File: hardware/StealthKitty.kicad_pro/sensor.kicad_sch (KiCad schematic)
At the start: 11 parts, among them J1 Conn_01x08, J7 Conn_01x06, J9 Conn_01x06, U5 ADXL343

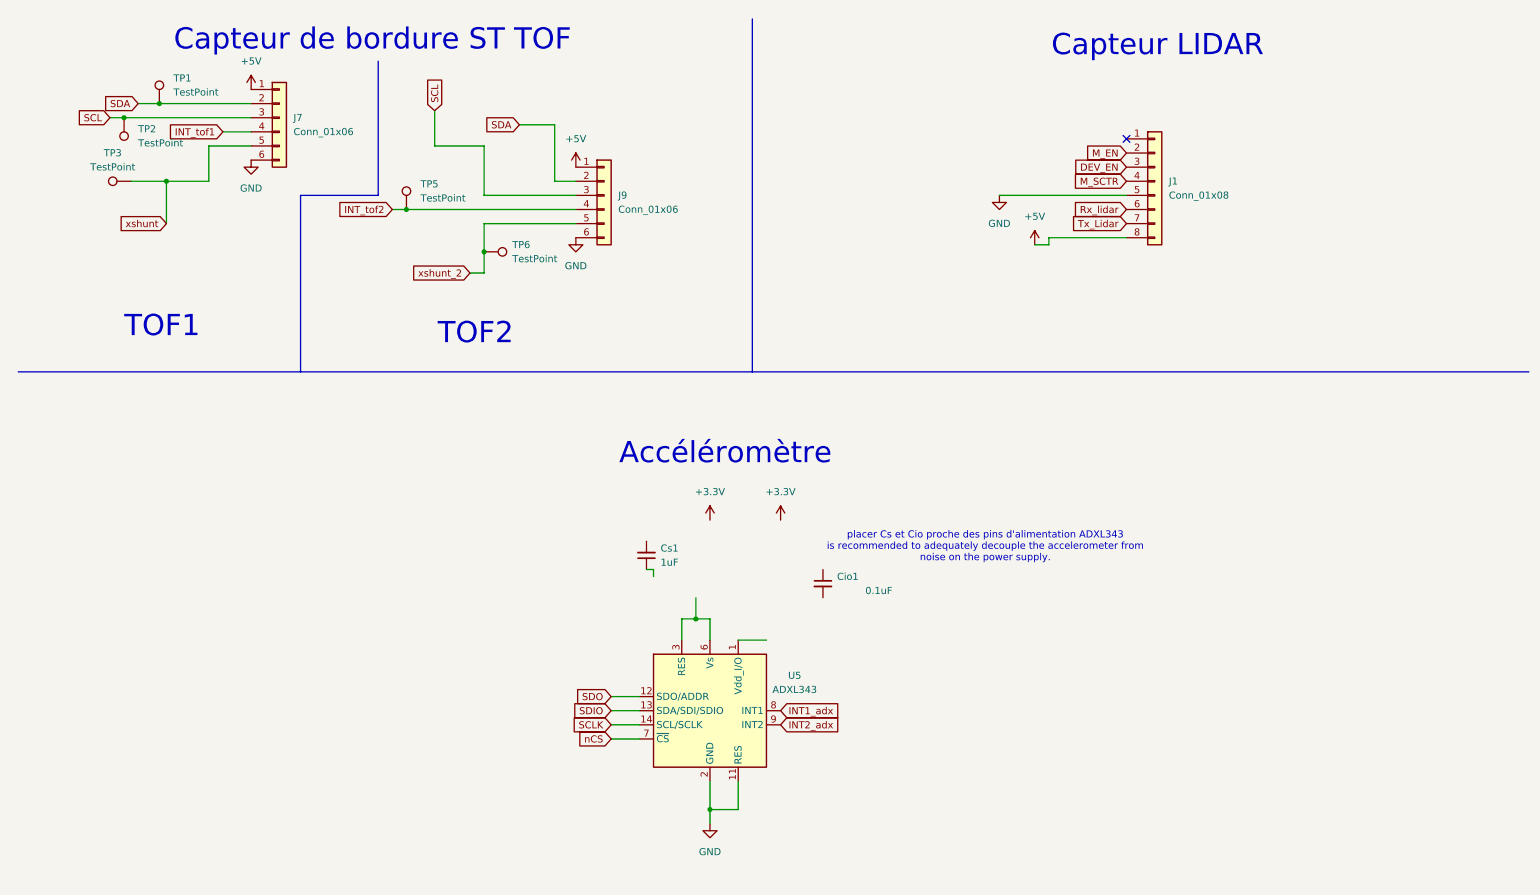
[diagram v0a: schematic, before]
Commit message: réassignation pins stm32, ajout des modifs de la partie power, ajout des modfis de la revue de projet 02/10/24, modifs du 3/10/24 voir readme
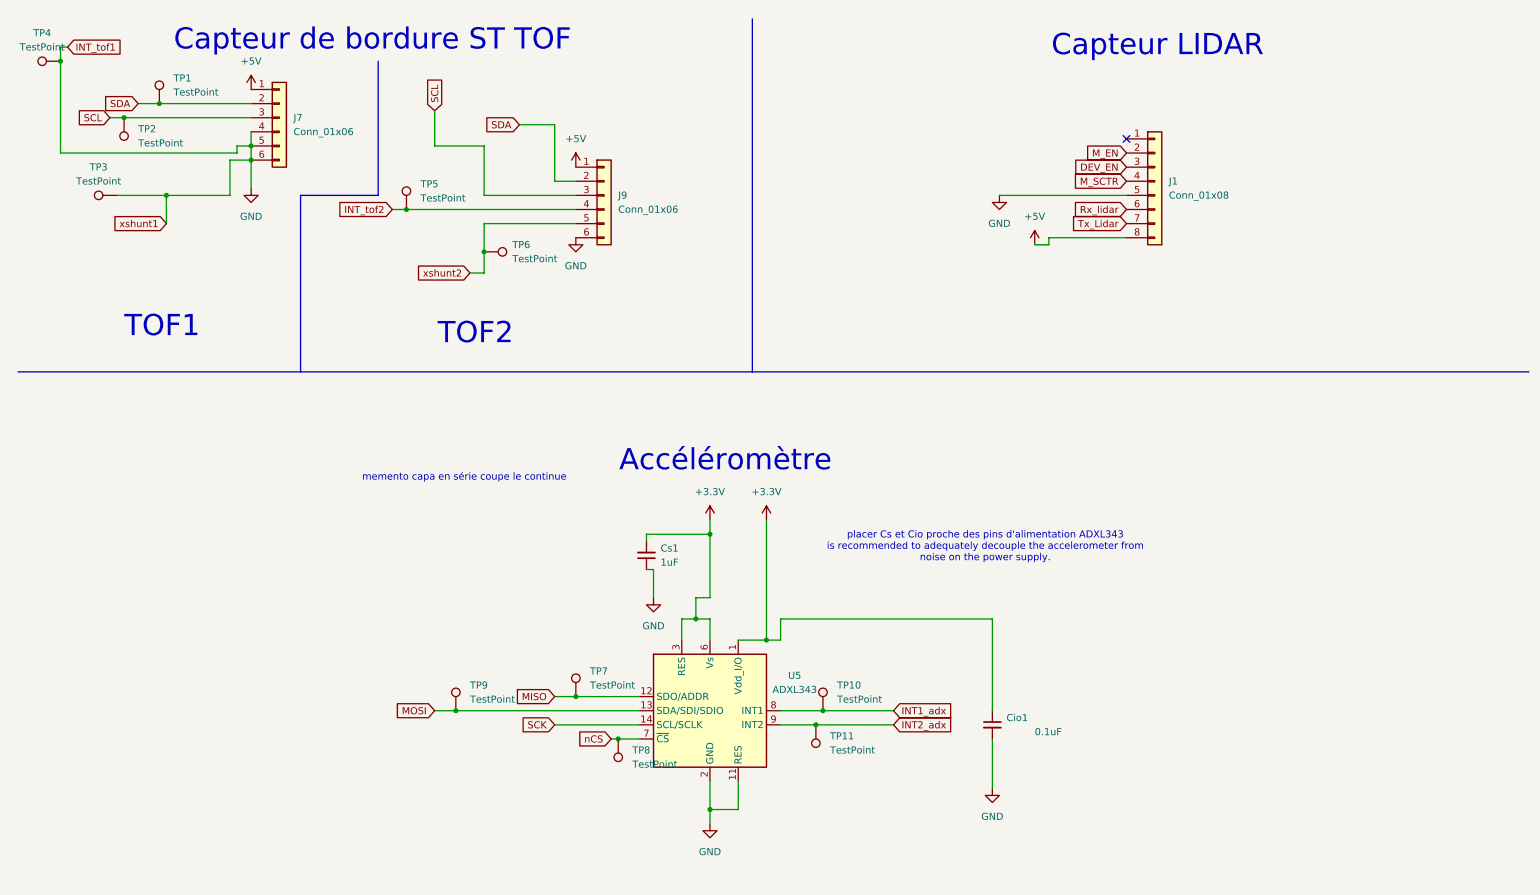
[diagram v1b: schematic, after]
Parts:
- added TP10, TP11, TP4, TP7, TP8, TP9: TestPoint, TestPoint:TestPoint_Pad_D1.5mm, symbol Connector:TestPoint
- TP1, TP2, TP3, TP5, TP6: footprint (none) -> TestPoint:TestPoint_Pad_D1.5mm
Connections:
- net INT_tof1 is gone; now on net GND: J7.4 (Pin_4)
- net xshunt is gone; now on net GND: J7.5 (Pin_5), TP3.1
- net +3.3V: now also Cio1.1, Cs1.2, U5.1 (Vdd_I/O), U5.3 (RES), U5.6 (Vs)
- net GND: now also Cio1.2, Cs1.1, TP4.1
- net INT1_adx: now also TP10.1
- net INT2_adx: now also TP11.1
- net nCS: now also TP8.1
- net SCLK renamed SCK
- net SDIO renamed MOSI
- net MOSI: now also TP9.1
- net SDO renamed MISO
- net MISO: now also TP7.1
- net xshunt_2 renamed xshunt2
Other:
- note added: "memento capa en série coupe le continue"
- moved on the sheet: Cio1, TP3

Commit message: MAJ routage equipe
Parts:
- removed TP8: TestPoint, TestPoint:TestPoint_Pad_D1.5mm, symbol Connector:TestPoint
- Cio1: footprint (none) -> Capacitor_SMD:C_0402_1005Metric_Pad0.74x0.62mm_HandSolder
- Cs1: footprint (none) -> Capacitor_SMD:C_0603_1608Metric_Pad1.08x0.95mm_HandSolder
- J7, J9: footprint (none) -> Connector_JST:JST_XH_B6B-XH-A_1x06_P2.50mm_Vertical
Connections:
- net GND: no longer J7.4 (Pin_4), J7.5 (Pin_5), TP3.1, TP4.1
- new net INT_tof1: J7.4 (Pin_4), TP4.1
- new net xshunt1: J7.5 (Pin_5), TP3.1
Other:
- moved on the sheet: Cio1, J7, J9, TP1, TP2, TP3, TP4, TP5, TP6, TP9

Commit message: Confirmation placement equipe
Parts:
- renumbered Cio1 to Cio301, Cs1 to Cs301, J7 to J301, J9 to J302, J1 to J303, TP4 to TP301, TP3 to TP302, TP1 to TP303, TP2 to TP304, TP5 to TP305, TP6 to TP306, TP7 to TP307, TP9 to TP308, TP11 to TP309, TP10 to TP310, U5 to U301
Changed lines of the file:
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@@
 		(dnp no)
 		(fields_autoplaced yes)
-		(property "Reference" "#PWR061"
+		(property "Reference" "#PWR0308"
 			(at 142.24 106.68 0)
 			(effects
@@
 			(project "StealthKitty.kicad_pro"
 				(path "/23d5732b-7ccb-40aa-85a2-3b18421ac23b/8cd8413a-9ba4-4bd6-b413-2331caa50cc2"
-					(reference "#PWR061")
+					(reference "#PWR0308")
 					(unit 1)
 				)
@@
 		(on_board yes)
 		(dnp no)
-		(property "Reference" "TP1"
+		(property "Reference" "TP303"
 			(at 48.006 23.876 0)
 			(effects
@@
 			(project "StealthKitty.kicad_pro"
 				(path "/23d5732b-7ccb-40aa-85a2-3b18421ac23b/8cd8413a-9ba4-4bd6-b413-2331caa50cc2"
-					(reference "TP1")
+					(reference "TP303")
 					(unit 1)
 				)
@@
 		(dnp no)
 		(fields_autoplaced yes)
-		(property "Reference" "TP7"
+		(property "Reference" "TP307"
 			(at 115.57 130.0479 0)
 			(effects
@@
 			(project "StealthKitty.kicad_pro"
 				(path "/23d5732b-7ccb-40aa-85a2-3b18421ac23b/8cd8413a-9ba4-4bd6-b413-2331caa50cc2"
-					(reference "TP7")
+					(reference "TP307")
 					(unit 1)
 				)
@@
 		(dnp no)
 		(fields_autoplaced yes)
-		(property "Reference" "#PWR01"
+		(property "Reference" "#PWR0302"
 			(at 58.42 53.34 0)
 			(effects
@@
 			(project "StealthKitty.kicad_pro"
 				(path "/23d5732b-7ccb-40aa-85a2-3b18421ac23b/8cd8413a-9ba4-4bd6-b413-2331caa50cc2"
-					(reference "#PWR01")
+					(reference "#PWR0302")
 					(unit 1)
 				)
@@
 		(on_board yes)
 		(dnp no)
-		(property "Reference" "TP2"
+		(property "Reference" "TP304"
 			(at 44.45 35.814 0)
 			(effects
@@
 			(project "StealthKitty.kicad_pro"
 				(path "/23d5732b-7ccb-40aa-85a2-3b18421ac23b/8cd8413a-9ba4-4bd6-b413-2331caa50cc2"
-					(reference "TP2")
+					(reference "TP304")
 					(unit 1)
 				)
@@
 		(on_board yes)
 		(dnp no)
-		(property "Reference" "#PWR023"
+		(property "Reference" "#PWR0301"
 			(at 54.61 33.02 0)
 			(effects
@@
 			(project "StealthKitty.kicad_pro"
 				(path "/23d5732b-7ccb-40aa-85a2-3b18421ac23b/8cd8413a-9ba4-4bd6-b413-2331caa50cc2"
-					(reference "#PWR023")
+					(reference "#PWR0301")
 					(unit 1)
 				)
@@
 		(dnp no)
 		(fields_autoplaced yes)
-		(property "Reference" "J9"
+		(property "Reference" "J302"
 			(at 130.81 34.2899 0)
 			(effects
@@
 			(project "StealthKitty.kicad_pro"
 				(path "/23d5732b-7ccb-40aa-85a2-3b18421ac23b/8cd8413a-9ba4-4bd6-b413-2331caa50cc2"
-					(reference "J9")
+					(reference "J302")
 					(unit 1)
 				)
@@
 		(dnp no)
 		(fields_autoplaced yes)
-		(property "Reference" "#PWR060"
+		(property "Reference" "#PWR0304"
 			(at 123.19 48.26 0)
 			(effects
@@
 			(project "StealthKitty.kicad_pro"
 				(path "/23d5732b-7ccb-40aa-85a2-3b18421ac23b/8cd8413a-9ba4-4bd6-b413-2331caa50cc2"
-					(reference "#PWR060")
+					(reference "#PWR0304")
 					(unit 1)
 				)
@@
 		(dnp no)
 		(fields_autoplaced yes)
-		(property "Reference" "J1"
+		(property "Reference" "J303"
 			(at 219.71 41.9099 0)
 			(effects
@@
 			(project "StealthKitty.kicad_pro"
 				(path "/23d5732b-7ccb-40aa-85a2-3b18421ac23b/8cd8413a-9ba4-4bd6-b413-2331caa50cc2"
-					(reference "J1")
+					(reference "J303")
 					(unit 1)
 				)
@@
 		(dnp no)
 		(fields_autoplaced yes)
-		(property "Reference" "#PWR022"
+		(property "Reference" "#PWR0311"
 			(at 195.58 55.88 0)
 			(effects
@@
 			(project "StealthKitty.kicad_pro"
 				(path "/23d5732b-7ccb-40aa-85a2-3b18421ac23b/8cd8413a-9ba4-4bd6-b413-2331caa50cc2"
-					(reference "#PWR022")
+					(reference "#PWR0311")
 					(unit 1)
 				)
@@
 		(dnp no)
 		(fields_autoplaced yes)
-		(property "Reference" "TP6"
+		(property "Reference" "TP306"
 			(at 105.41 46.4819 0)
 			(effects
@@
 			(project "StealthKitty.kicad_pro"
 				(path "/23d5732b-7ccb-40aa-85a2-3b18421ac23b/8cd8413a-9ba4-4bd6-b413-2331caa50cc2"
-					(reference "TP6")
+					(reference "TP306")
 					(unit 1)
 				)
@@
 		(dnp no)
 		(fields_autoplaced yes)
-		(property "Reference" "TP10"
+		(property "Reference" "TP310"
 			(at 160.02 132.5879 0)
 			(effects
@@
 			(project "StealthKitty.kicad_pro"
 				(path "/23d5732b-7ccb-40aa-85a2-3b18421ac23b/8cd8413a-9ba4-4bd6-b413-2331caa50cc2"
-					(reference "TP10")
+					(reference "TP310")
 					(unit 1)
 				)
@@
 		(dnp no)
 		(fields_autoplaced yes)
-		(property "Reference" "#PWR059"
+		(property "Reference" "#PWR0303"
 			(at 123.19 33.02 0)
 			(effects
@@
 			(project "StealthKitty.kicad_pro"
 				(path "/23d5732b-7ccb-40aa-85a2-3b18421ac23b/8cd8413a-9ba4-4bd6-b413-2331caa50cc2"
-					(reference "#PWR059")
+					(reference "#PWR0303")
 					(unit 1)
 				)
@@
 		(dnp no)
 		(fields_autoplaced yes)
-		(property "Reference" "#PWR062"
+		(property "Reference" "#PWR0310"
 			(at 189.23 50.8 0)
 			(effects
@@
 			(project "StealthKitty.kicad_pro"
 				(path "/23d5732b-7ccb-40aa-85a2-3b18421ac23b/8cd8413a-9ba4-4bd6-b413-2331caa50cc2"
-					(reference "#PWR062")
+					(reference "#PWR0310")
 					(unit 1)
 				)
@@
 		(on_board yes)
 		(dnp no)
-		(property "Reference" "TP3"
+		(property "Reference" "TP302"
 			(at 29.464 51.054 0)
 			(effects
@@
 			(project "StealthKitty.kicad_pro"
 				(path "/23d5732b-7ccb-40aa-85a2-3b18421ac23b/8cd8413a-9ba4-4bd6-b413-2331caa50cc2"
-					(reference "TP3")
+					(reference "TP302")
 					(unit 1)
 				)
@@
 		(dnp no)
 		(fields_autoplaced yes)
-		(property "Reference" "U5"
+		(property "Reference" "U301"
 			(at 152.4 130.8414 0)
 			(effects
@@
 			(project "StealthKitty.kicad_pro"
 				(path "/23d5732b-7ccb-40aa-85a2-3b18421ac23b/8cd8413a-9ba4-4bd6-b413-2331caa50cc2"
-					(reference "U5")
+					(reference "U301")
 					(unit 1)
 				)
@@
 		(dnp no)
 		(fields_autoplaced yes)
-		(property "Reference" "J7"
+		(property "Reference" "J301"
 			(at 66.04 34.2899 0)
 			(effects
@@
 			(project "StealthKitty.kicad_pro"
 				(path "/23d5732b-7ccb-40aa-85a2-3b18421ac23b/8cd8413a-9ba4-4bd6-b413-2331caa50cc2"
-					(reference "J7")
+					(reference "J301")
 					(unit 1)
 				)
@@
 		(dnp no)
 		(fields_autoplaced yes)
-		(property "Reference" "#PWR058"
+		(property "Reference" "#PWR0307"
 			(at 137.16 163.83 0)
 			(effects
@@
 			(project "StealthKitty.kicad_pro"
 				(path "/23d5732b-7ccb-40aa-85a2-3b18421ac23b/8cd8413a-9ba4-4bd6-b413-2331caa50cc2"
-					(reference "#PWR058")
+					(reference "#PWR0307")
 					(unit 1)
 				)
@@
 		(dnp no)
 		(fields_autoplaced yes)
-		(property "Reference" "#PWR035"
+		(property "Reference" "#PWR0305"
 			(at 125.73 121.92 0)
 			(effects
@@
 			(project "StealthKitty.kicad_pro"
 				(path "/23d5732b-7ccb-40aa-85a2-3b18421ac23b/8cd8413a-9ba4-4bd6-b413-2331caa50cc2"
-					(reference "#PWR035")
+					(reference "#PWR0305")
 					(unit 1)
 				)
@@
 		(on_board yes)
 		(dnp no)
-		(property "Reference" "TP9"
+		(property "Reference" "TP308"
 			(at 118.364 148.082 0)
 			(effects
@@
 			(project "StealthKitty.kicad_pro"
 				(path "/23d5732b-7ccb-40aa-85a2-3b18421ac23b/8cd8413a-9ba4-4bd6-b413-2331caa50cc2"
-					(reference "TP9")
+					(reference "TP308")
 					(unit 1)
 				)
@@
 		(dnp no)
 		(fields_autoplaced yes)
-		(property "Reference" "#PWR025"
+		(property "Reference" "#PWR0306"
 			(at 134.62 106.68 0)
 			(effects
@@
 			(project "StealthKitty.kicad_pro"
 				(path "/23d5732b-7ccb-40aa-85a2-3b18421ac23b/8cd8413a-9ba4-4bd6-b413-2331caa50cc2"
-					(reference "#PWR025")
+					(reference "#PWR0306")
 					(unit 1)
 				)
@@
 		(on_board yes)
 		(dnp no)
-		(property "Reference" "Cs1"
+		(property "Reference" "Cs301"
 			(at 128.27 107.9435 0)
 			(effects
@@
 			(project "StealthKitty.kicad_pro"
 				(path "/23d5732b-7ccb-40aa-85a2-3b18421ac23b/8cd8413a-9ba4-4bd6-b413-2331caa50cc2"
-					(reference "Cs1")
+					(reference "Cs301")
 					(unit 1)
 				)
@@
 		(on_board yes)
 		(dnp no)
-		(property "Reference" "TP5"
+		(property "Reference" "TP305"
 			(at 98.298 28.448 0)
 			(effects
@@
 			(project "StealthKitty.kicad_pro"
 				(path "/23d5732b-7ccb-40aa-85a2-3b18421ac23b/8cd8413a-9ba4-4bd6-b413-2331caa50cc2"
-					(reference "TP5")
+					(reference "TP305")
 					(unit 1)
 				)
@@
 		(on_board yes)
 		(dnp no)
-		(property "Reference" "Cio1"
+		(property "Reference" "Cio301"
 			(at 154.94 107.9562 0)
 			(effects
@@
 			(project "StealthKitty.kicad_pro"
 				(path "/23d5732b-7ccb-40aa-85a2-3b18421ac23b/8cd8413a-9ba4-4bd6-b413-2331caa50cc2"
-					(reference "Cio1")
+					(reference "Cio301")
 					(unit 1)
 				)
@@
 		(on_board yes)
 		(dnp no)
-		(property "Reference" "TP4"
+		(property "Reference" "TP301"
 			(at 31.242 34.544 0)
 			(effects
@@
 			(project "StealthKitty.kicad_pro"
 				(path "/23d5732b-7ccb-40aa-85a2-3b18421ac23b/8cd8413a-9ba4-4bd6-b413-2331caa50cc2"
-					(reference "TP4")
+					(reference "TP301")
 					(unit 1)
 				)
@@
 		(dnp no)
 		(fields_autoplaced yes)
-		(property "Reference" "TP11"
+		(property "Reference" "TP309"
 			(at 158.75 141.7319 0)
 			(effects
@@
 			(project "StealthKitty.kicad_pro"
 				(path "/23d5732b-7ccb-40aa-85a2-3b18421ac23b/8cd8413a-9ba4-4bd6-b413-2331caa50cc2"
-					(reference "TP11")
+					(reference "TP309")
 					(unit 1)
 				)
@@
 		(dnp no)
 		(fields_autoplaced yes)
-		(property "Reference" "#PWR034"
+		(property "Reference" "#PWR0309"
 			(at 152.4 121.92 0)
 			(effects
@@
 			(project "StealthKitty.kicad_pro"
 				(path "/23d5732b-7ccb-40aa-85a2-3b18421ac23b/8cd8413a-9ba4-4bd6-b413-2331caa50cc2"
-					(reference "#PWR034")
-					(unit 1)
-				)
+					(reference "#PWR0309")
+					(unit 1)
+				)

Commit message: Dernier Modif 08/10/2024
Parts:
- removed TP303, TP304, TP306: TestPoint, TestPoint:TestPoint_Pad_D1.5mm, symbol Connector:TestPoint
- Cio301: footprint Capacitor_SMD:C_0402_1005Metric_Pad0.74x0.62mm_HandSolder -> Capacitor_SMD:C_0402_1005Metric
- Cs301: footprint Capacitor_SMD:C_0603_1608Metric_Pad1.08x0.95mm_HandSolder -> Capacitor_SMD:C_0402_1005Metric
- J301, J302: footprint Connector_JST:JST_XH_B6B-XH-A_1x06_P2.50mm_Vertical -> Connector_JST:JST_XH_S6B-XH-A_1x06_P2.50mm_Horizontal
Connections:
- net INT_tof1: no longer TP301.1
- net SCK: now also TP301.1
- net nCS: now also TP302.1
- net xshunt1: no longer TP302.1
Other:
- moved on the sheet: TP308

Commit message: Modification Placement 09/10/24
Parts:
- removed TP305: TestPoint, TestPoint:TestPoint_Pad_D1.5mm, symbol Connector:TestPoint
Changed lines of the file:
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@@
-	)
-	(junction
-		(at 102.87 36.83)
-		(diameter 0)
-		(color 0 0 0 0)
 	)
 	(junction
@@
 	(wire
 		(pts
-			(xy 102.87 36.83) (xy 123.19 36.83)
+			(xy 99.06 36.83) (xy 123.19 36.83)
 		)
 		(stroke
@@
 	(wire
 		(pts
-			(xy 99.06 36.83) (xy 102.87 36.83)
-		)
-		(stroke
-			(width 0)
-			(type default)
-		)
-	)
-	(wire
-		(pts
 			(xy 110.49 29.21) (xy 110.49 34.29)
 		)
@@
 		(pts
 			(xy 52.07 39.37) (xy 58.42 39.37)
-		)
-		(stroke
-			(width 0)
-			(type default)
-		)
-	)
-	(wire
-		(pts
-			(xy 102.87 33.02) (xy 102.87 36.83)
 		)
 		(stroke
@@
 					(unit 1)
 				)
-			)
-		)
-	)
-	(symbol
-		(lib_id "Connector:TestPoint")
-		(at 102.87 33.02 0)
-		(unit 1)
-		(exclude_from_sim no)
-		(in_bom yes)
-		(on_board yes)
-		(dnp no)
-		(property "Reference" "TP305"
-			(at 98.298 28.448 0)
-			(effects
-				(font
-					(size 1.27 1.27)
-				)
-				(justify left)
-			)
-		)
-		(property "Value" "TestPoint"
-			(at 92.964 30.988 0)
-			(effects
-				(font
-					(size 1.27 1.27)
-				)
-				(justify left)
-			)
-		)
-		(property "Footprint" "TestPoint:TestPoint_Pad_D1.5mm"
-			(at 107.95 33.02 0)
-			(effects
-				(font
-					(size 1.27 1.27)
-				)
-				(hide yes)
-			)
-		)
-		(property "Datasheet" "~"
-			(at 107.95 33.02 0)
-			(effects
-				(font
-					(size 1.27 1.27)
-				)
-				(hide yes)
-			)
-		)
-		(property "Description" "test point"
-			(at 102.87 33.02 0)
-			(effects
-				(font
-					(size 1.27 1.27)
-				)
-				(hide yes)
-			)
-		)
-		(pin "1"
-		)
-		(instances
-			(project "StealthKitty.kicad_pro"
-				(path "/23d5732b-7ccb-40aa-85a2-3b18421ac23b/8cd8413a-9ba4-4bd6-b413-2331caa50cc2"
-					(reference "TP305")
-					(unit 1)
-				)

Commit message: CRCR
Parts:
- added TP305: TestPoint, TestPoint:TestPoint_Pad_D1.5mm, symbol Connector:TestPoint
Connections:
- net INT_tof2: now also TP305.1
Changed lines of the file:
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@@
+	)
+	(junction
+		(at 102.87 36.83)
+		(diameter 0)
+		(color 0 0 0 0)
 	)
 	(junction
@@
 	(wire
 		(pts
-			(xy 99.06 36.83) (xy 123.19 36.83)
+			(xy 102.87 36.83) (xy 123.19 36.83)
 		)
 		(stroke
@@
 	(wire
 		(pts
+			(xy 99.06 36.83) (xy 102.87 36.83)
+		)
+		(stroke
+			(width 0)
+			(type default)
+		)
+	)
+	(wire
+		(pts
 			(xy 110.49 29.21) (xy 110.49 34.29)
 		)
@@
 		(pts
 			(xy 52.07 39.37) (xy 58.42 39.37)
+		)
+		(stroke
+			(width 0)
+			(type default)
+		)
+	)
+	(wire
+		(pts
+			(xy 102.87 33.02) (xy 102.87 36.83)
 		)
 		(stroke
@@
 					(unit 1)
 				)
+			)
+		)
+	)
+	(symbol
+		(lib_id "Connector:TestPoint")
+		(at 102.87 33.02 0)
+		(unit 1)
+		(exclude_from_sim no)
+		(in_bom yes)
+		(on_board yes)
+		(dnp no)
+		(property "Reference" "TP305"
+			(at 98.298 28.448 0)
+			(effects
+				(font
+					(size 1.27 1.27)
+				)
+				(justify left)
+			)
+		)
+		(property "Value" "TestPoint"
+			(at 92.964 30.988 0)
+			(effects
+				(font
+					(size 1.27 1.27)
+				)
+				(justify left)
+			)
+		)
+		(property "Footprint" "TestPoint:TestPoint_Pad_D1.5mm"
+			(at 107.95 33.02 0)
+			(effects
+				(font
+					(size 1.27 1.27)
+				)
+				(hide yes)
+			)
+		)
+		(property "Datasheet" "~"
+			(at 107.95 33.02 0)
+			(effects
+				(font
+					(size 1.27 1.27)
+				)
+				(hide yes)
+			)
+		)
+		(property "Description" "test point"
+			(at 102.87 33.02 0)
+			(effects
+				(font
+					(size 1.27 1.27)
+				)
+				(hide yes)
+			)
+		)
+		(pin "1"
+		)
+		(instances
+			(project "StealthKitty.kicad_pro"
+				(path "/23d5732b-7ccb-40aa-85a2-3b18421ac23b/8cd8413a-9ba4-4bd6-b413-2331caa50cc2"
+					(reference "TP305")
+					(unit 1)
+				)
